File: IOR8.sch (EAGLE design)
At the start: 54 parts, among them Q1 2N7002, Q2 2N7002, Q3 2N7002, Q4 2N7002, Q5 2N7002, Q6 2N7002, Q7 2N7002, Q8 2N7002

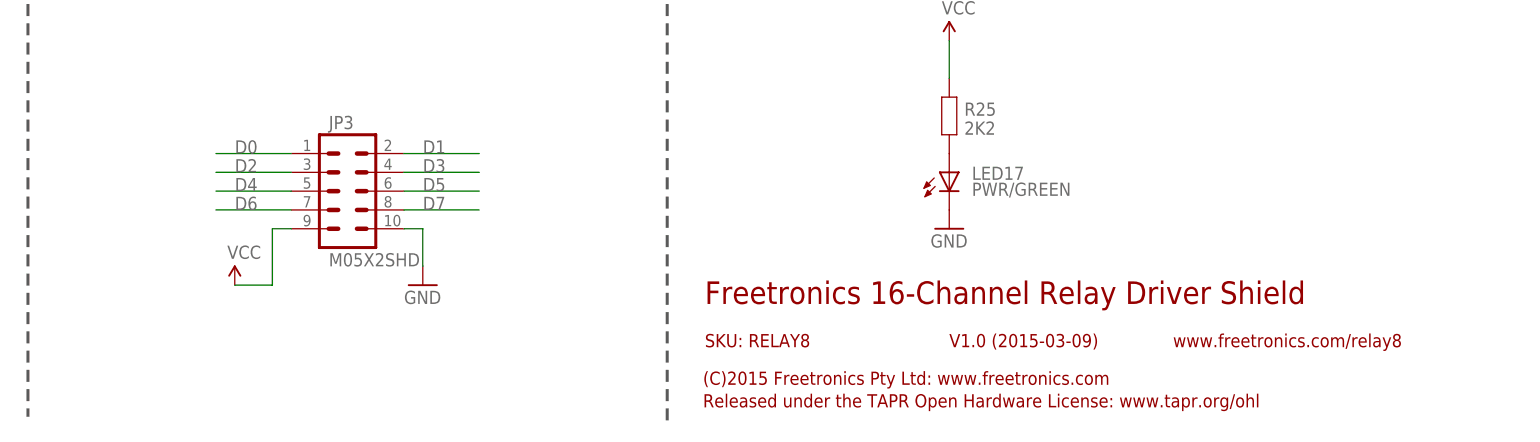
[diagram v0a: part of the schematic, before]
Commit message: Expanded headers to 2x6 to include IOREF and RESET for v2.0 release
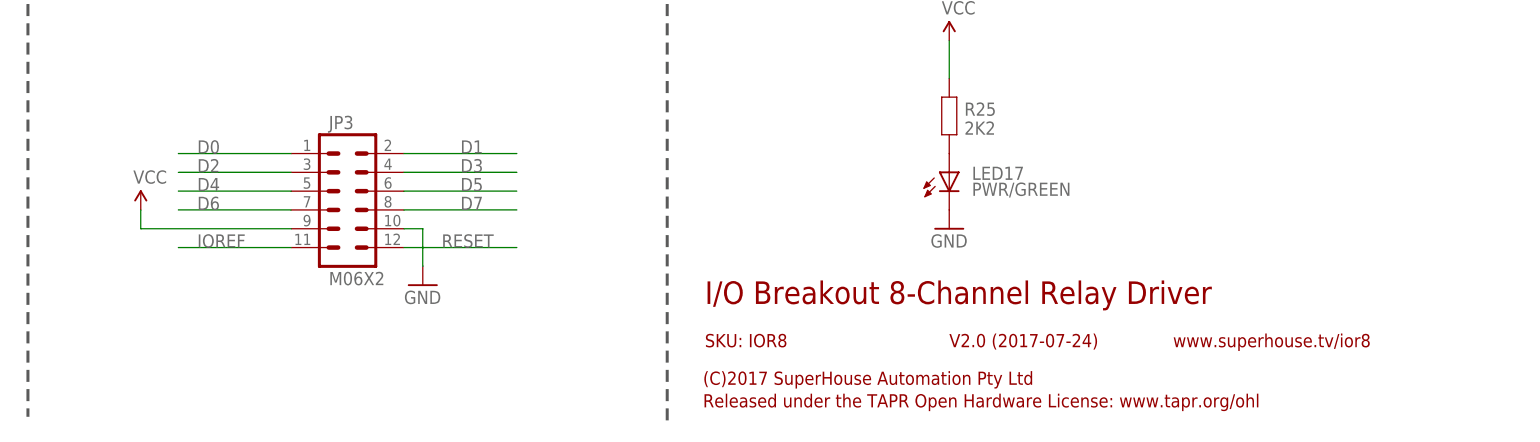
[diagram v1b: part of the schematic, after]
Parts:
- JP3: value M05X2SHD -> M06X2; device freetronics-original:M05X2SHD -> freetronics-jon:M06X2
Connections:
- new net IOREF: JP3.11
- new net RESET: JP3.12
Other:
- note added: "(C)2017 SuperHouse Automation Pty Ltd"
- note added: "I/O Breakout 8-Channel Relay Driver"
- note added: "SKU: IOR8"
- note added: "V2.0 (2017-07-24)"
- note added: "www.superhouse.tv/ior8"
- note removed: "(C)2015 Freetronics Pty Ltd: www.freetronics.com"
- note removed: "Freetronics 16-Channel Relay Driver Shield"
- note removed: "SKU: RELAY8"
- note removed: "V1.0 (2015-03-09)"
- note removed: "www.freetronics.com/relay8"
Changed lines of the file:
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@@
 <layer number="54" name="bGND_GNDA" color="1" fill="9" visible="no" active="no"/>
 <layer number="56" name="wert" color="7" fill="1" visible="no" active="no"/>
+<layer number="57" name="tCAD" color="7" fill="1" visible="no" active="no"/>
+<layer number="59" name="tCarbon" color="7" fill="1" visible="no" active="no"/>
+<layer number="60" name="bCarbon" color="7" fill="1" visible="no" active="no"/>
+<layer number="90" name="Modules" color="7" fill="1" visible="yes" active="yes"/>
 <layer number="91" name="Nets" color="2" fill="1" visible="yes" active="yes"/>
 <layer number="92" name="Busses" color="1" fill="1" visible="yes" active="yes"/>
@@
 <layer number="97" name="Info" color="7" fill="1" visible="yes" active="yes"/>
 <layer number="98" name="Guide" color="6" fill="1" visible="yes" active="yes"/>
+<layer number="99" name="SpiceOrder" color="7" fill="1" visible="no" active="no"/>
 <layer number="100" name="Muster" color="7" fill="1" visible="no" active="no"/>
 <layer number="101" name="Patch_Top" color="12" fill="4" visible="yes" active="yes"/>
@@
 <layer number="111" name="LPC17xx" color="7" fill="1" visible="yes" active="yes"/>
 <layer number="112" name="tSilk" color="7" fill="1" visible="yes" active="yes"/>
+<layer number="113" name="ReferenceLS" color="7" fill="1" visible="no" active="no"/>
 <layer number="116" name="Patch_BOT" color="9" fill="4" visible="yes" active="yes"/>
+<layer number="118" name="Rect_Pads" color="7" fill="1" visible="no" active="no"/>
 <layer number="121" name="_tsilk" color="7" fill="1" visible="yes" active="yes"/>
 <layer number="122" name="_bsilk" color="7" fill="1" visible="yes" active="yes"/>
@@
 <layer number="127" name="_tValues" color="7" fill="1" visible="yes" active="yes"/>
 <layer number="128" name="_bValues" color="7" fill="1" visible="yes" active="yes"/>
+<layer number="129" name="Mask" color="7" fill="1" visible="yes" active="yes"/>
 <layer number="131" name="tAdjust" color="7" fill="1" visible="yes" active="yes"/>
 <layer number="132" name="bAdjust" color="7" fill="1" visible="yes" active="yes"/>
 <layer number="144" name="Drill_legend" color="7" fill="1" visible="yes" active="yes"/>
+<layer number="150" name="Notes" color="7" fill="1" visible="yes" active="yes"/>
 <layer number="151" name="HeatSink" color="7" fill="1" visible="yes" active="yes"/>
 <layer number="152" name="_bDocu" color="7" fill="1" visible="yes" active="yes"/>
+<layer number="153" name="FabDoc1" color="6" fill="1" visible="no" active="no"/>
+<layer number="154" name="FabDoc2" color="2" fill="1" visible="no" active="no"/>
+<layer number="155" name="FabDoc3" color="7" fill="15" visible="no" active="no"/>
 <layer number="199" name="Contour" color="7" fill="1" visible="yes" active="yes"/>
 <layer number="200" name="200bmp" color="1" fill="10" visible="no" active="no"/>
@@
 <layer number="223" name="223bmp" color="7" fill="1" visible="yes" active="yes"/>
 <layer number="224" name="224bmp" color="7" fill="1" visible="yes" active="yes"/>
+<layer number="225" name="225bmp" color="7" fill="1" visible="yes" active="yes"/>
+<layer number="226" name="226bmp" color="7" fill="1" visible="yes" active="yes"/>
+<layer number="227" name="227bmp" color="7" fill="1" visible="yes" active="yes"/>
+<layer number="228" name="228bmp" color="7" fill="1" visible="yes" active="yes"/>
+<layer number="229" name="229bmp" color="7" fill="1" visible="yes" active="yes"/>
+<layer number="230" name="230bmp" color="7" fill="1" visible="yes" active="yes"/>
 <layer number="231" name="Eagle3D_PG1" color="7" fill="1" visible="yes" active="yes"/>
 <layer number="232" name="Eagle3D_PG2" color="7" fill="1" visible="yes" active="yes"/>
@@
 <layer number="251" name="SMDround" color="12" fill="11" visible="no" active="no"/>
 <layer number="254" name="cooling" color="7" fill="1" visible="yes" active="yes"/>
+<layer number="255" name="routoute" color="7" fill="1" visible="yes" active="yes"/>
 </layers>
 <schematic xreflabel="%F%N/%S.%C%R" xrefpart="/%S.%C%R">
@@
 <part name="JP1" library="freetronics-master-v1" deviceset="M08" device=""/>
 <part name="JP2" library="freetronics-master-v1" deviceset="M08" device=""/>
-<part name="JP3" library="freetronics-original" deviceset="M05X2" device="SHD"/>
+<part name="JP3" library="freetronics-jon" deviceset="M06X2" device=""/>
 <part name="GND2" library="freetronics" deviceset="GND" device=""/>
 <part name="P+1" library="freetronics-original" deviceset="VCC" device=""/>
@@
 <wire x1="129.54" y1="66.04" x2="129.54" y2="3.81" width="0.4064" layer="97" style="longdash"/>
 <wire x1="43.18" y1="66.04" x2="43.18" y2="5.08" width="0.4064" layer="97" style="longdash"/>
-<text x="134.62" y="20.32" size="3.048" layer="94">Freetronics 16-Channel Relay Driver Shield</text>
-<text x="167.64" y="14.478" size="1.778" layer="94">V1.0 (2015-03-09)</text>
-<text x="134.62" y="14.478" size="1.778" layer="94">SKU: RELAY8</text>
-<text x="134.366" y="9.398" size="1.778" layer="94">(C)2015 Freetronics Pty Ltd: www.freetronics.com</text>
+<text x="134.62" y="20.32" size="3.048" layer="94">I/O Breakout 8-Channel Relay Driver</text>
+<text x="167.64" y="14.478" size="1.778" layer="94">V2.0 (2017-07-24)</text>
+<text x="134.62" y="14.478" size="1.778" layer="94">SKU: IOR8</text>
+<text x="134.366" y="9.398" size="1.778" layer="94">(C)2017 SuperHouse Automation Pty Ltd</text>
 <text x="134.366" y="6.35" size="1.778" layer="94">Released under the TAPR Open Hardware License: www.tapr.org/ohl</text>
-<text x="197.866" y="14.478" size="1.778" layer="94">www.freetronics.com/relay8</text>
+<text x="197.866" y="14.478" size="1.778" layer="94">www.superhouse.tv/ior8</text>
 <text x="53.34" y="157.48" size="5.08" layer="94" ratio="12">1</text>
 <text x="53.34" y="129.54" size="5.08" layer="94" ratio="12">2</text>
@@
 <instance part="JP3" gate="G$1" x="86.36" y="35.56"/>
 <instance part="GND2" gate="1" x="96.52" y="22.86"/>
-<instance part="P+1" gate="1" x="71.12" y="22.86"/>
+<instance part="P+1" gate="1" x="58.42" y="33.02"/>
 <instance part="P+2" gate="1" x="50.8" y="91.44"/>
 <instance part="P+3" gate="1" x="50.8" y="119.38"/>
@@
 <segment>
 <pinref part="JP3" gate="G$1" pin="1"/>
-<wire x1="78.74" y1="40.64" x2="68.58" y2="40.64" width="0.1524" layer="91"/>
-<label x="71.12" y="40.64" size="1.778" layer="95"/>
+<wire x1="78.74" y1="40.64" x2="63.5" y2="40.64" width="0.1524" layer="91"/>
+<label x="66.04" y="40.64" size="1.778" layer="95"/>
 </segment>
 <segment>
@@
 <segment>
 <pinref part="JP3" gate="G$1" pin="2"/>
-<wire x1="93.98" y1="40.64" x2="104.14" y2="40.64" width="0.1524" layer="91"/>
-<label x="96.52" y="40.64" size="1.778" layer="95"/>
+<wire x1="93.98" y1="40.64" x2="109.22" y2="40.64" width="0.1524" layer="91"/>
+<label x="101.6" y="40.64" size="1.778" layer="95"/>
 </segment>
 <segment>
@@
 <segment>
 <pinref part="JP3" gate="G$1" pin="3"/>
-<wire x1="78.74" y1="38.1" x2="68.58" y2="38.1" width="0.1524" layer="91"/>
-<label x="71.12" y="38.1" size="1.778" layer="95"/>
+<wire x1="78.74" y1="38.1" x2="63.5" y2="38.1" width="0.1524" layer="91"/>
+<label x="66.04" y="38.1" size="1.778" layer="95"/>
 </segment>
 <segment>
@@
 <segment>
 <pinref part="JP3" gate="G$1" pin="9"/>
-<wire x1="78.74" y1="30.48" x2="76.2" y2="30.48" width="0.1524" layer="91"/>
-<wire x1="76.2" y1="30.48" x2="76.2" y2="22.86" width="0.1524" layer="91"/>
-<wire x1="76.2" y1="22.86" x2="71.12" y2="22.86" width="0.1524" layer="91"/>
+<wire x1="78.74" y1="30.48" x2="58.42" y2="30.48" width="0.1524" layer="91"/>
+<wire x1="58.42" y1="30.48" x2="58.42" y2="33.02" width="0.1524" layer="91"/>
 <pinref part="P+1" gate="1" pin="VCC"/>
 </segment>
@@
 <segment>
 <pinref part="JP3" gate="G$1" pin="5"/>
-<wire x1="68.58" y1="35.56" x2="78.74" y2="35.56" width="0.1524" layer="91"/>
-<label x="71.12" y="35.56" size="1.778" layer="95"/>
+<wire x1="63.5" y1="35.56" x2="78.74" y2="35.56" width="0.1524" layer="91"/>
+<label x="66.04" y="35.56" size="1.778" layer="95"/>
 </segment>
 <segment>
@@
 <segment>
 <pinref part="JP3" gate="G$1" pin="7"/>
-<wire x1="78.74" y1="33.02" x2="68.58" y2="33.02" width="0.1524" layer="91"/>
-<label x="71.12" y="33.02" size="1.778" layer="95"/>
+<wire x1="78.74" y1="33.02" x2="63.5" y2="33.02" width="0.1524" layer="91"/>
+<label x="66.04" y="33.02" size="1.778" layer="95"/>
 </segment>
 <segment>
@@
 <segment>
 <pinref part="JP3" gate="G$1" pin="8"/>
-<wire x1="93.98" y1="33.02" x2="104.14" y2="33.02" width="0.1524" layer="91"/>
-<label x="96.52" y="33.02" size="1.778" layer="95"/>
+<wire x1="93.98" y1="33.02" x2="109.22" y2="33.02" width="0.1524" layer="91"/>
+<label x="101.6" y="33.02" size="1.778" layer="95"/>
 </segment>
 <segment>
@@
 <segment>
 <pinref part="JP3" gate="G$1" pin="6"/>
-<wire x1="93.98" y1="35.56" x2="104.14" y2="35.56" width="0.1524" layer="91"/>
-<label x="96.52" y="35.56" size="1.778" layer="95"/>
+<wire x1="93.98" y1="35.56" x2="109.22" y2="35.56" width="0.1524" layer="91"/>
+<label x="101.6" y="35.56" size="1.778" layer="95"/>
 </segment>
 <segment>
@@
 <segment>
 <pinref part="JP3" gate="G$1" pin="4"/>
-<wire x1="93.98" y1="38.1" x2="104.14" y2="38.1" width="0.1524" layer="91"/>
-<label x="96.52" y="38.1" size="1.778" layer="95"/>
+<wire x1="93.98" y1="38.1" x2="109.22" y2="38.1" width="0.1524" layer="91"/>
+<label x="101.6" y="38.1" size="1.778" layer="95"/>
 </segment>
 <segment>
@@
 </segment>
 </net>
+<net name="RESET" class="0">
+<segment>
+<pinref part="JP3" gate="G$1" pin="12"/>
+<wire x1="93.98" y1="27.94" x2="109.22" y2="27.94" width="0.1524" layer="91"/>
+<label x="99.06" y="27.94" size="1.778" layer="95"/>
+</segment>
+</net>
+<net name="IOREF" class="0">
+<segment>
+<pinref part="JP3" gate="G$1" pin="11"/>
+<wire x1="78.74" y1="27.94" x2="63.5" y2="27.94" width="0.1524" layer="91"/>
+<label x="66.04" y="27.94" size="1.778" layer="95"/>
+</segment>
+</net>
